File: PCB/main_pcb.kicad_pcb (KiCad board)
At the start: 2 copper layers, 116.9 x 116.9 mm, 37 parts, among them P1 SEN, P2 SRV, P3 PWR, P4 LED, P5 M1, P6 M2, Q1 5LN01SP, U1 Teensy_3.1, U2 RFM69_Breakout, U3 MCP6004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

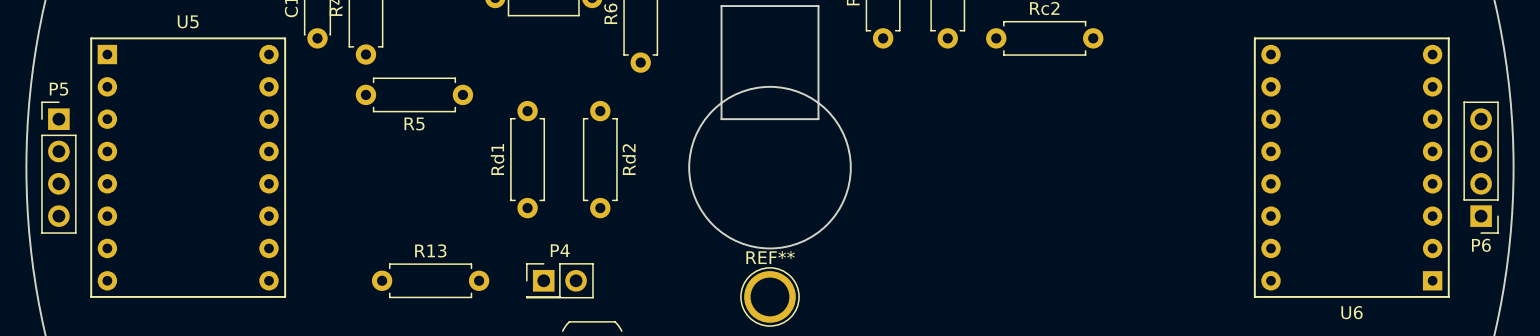
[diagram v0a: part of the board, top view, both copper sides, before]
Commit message: Added supporting PCB layouts
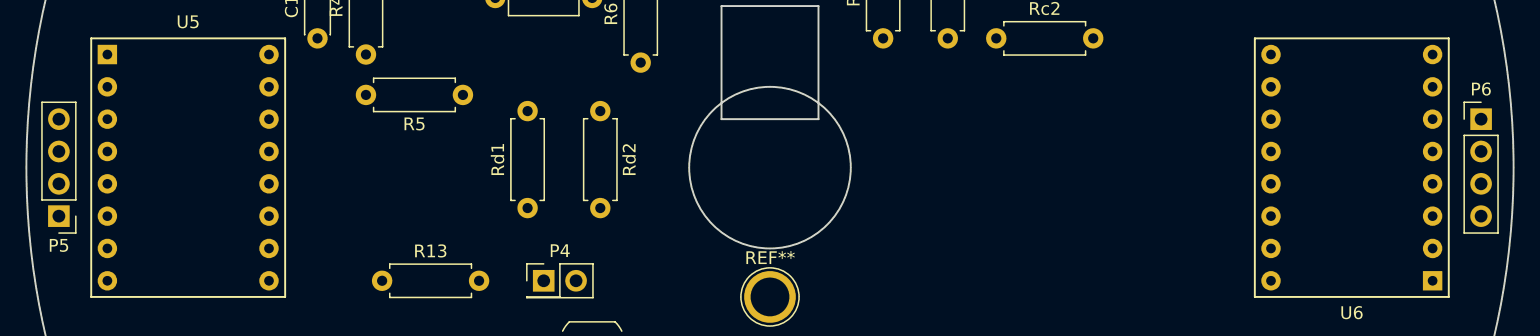
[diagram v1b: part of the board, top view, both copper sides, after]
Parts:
- moved P5 7.62 mm to (82.5, 99.1), turned to 180 degrees
- moved P6 7.62 mm to (194.3, 91.4), turned to 0 degrees
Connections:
- U5 pad 10: GND -> Net-(U5-Pad10)
- U5 pad 11: Net-(P5-Pad1) -> Net-(P5-Pad4)
- U5 pad 12: Net-(P5-Pad2) -> Net-(P5-Pad3)
- U5 pad 13: Net-(P5-Pad3) -> Net-(P5-Pad2)
- U5 pad 14: Net-(P5-Pad4) -> Net-(P5-Pad1)
- U5 pad 15: Net-(U5-Pad15) -> GND
- U5 pad 16: GND -> VDD
- U5 pad 9: VDD -> GND
- U6 pad 10: GND -> Net-(U6-Pad10)
- U6 pad 11: Net-(P6-Pad1) -> Net-(P6-Pad4)
- U6 pad 12: Net-(P6-Pad2) -> Net-(P6-Pad3)
- U6 pad 13: Net-(P6-Pad3) -> Net-(P6-Pad2)
- U6 pad 14: Net-(P6-Pad4) -> Net-(P6-Pad1)
- U6 pad 15: Net-(U6-Pad15) -> GND
- U6 pad 16: GND -> VDD
- U6 pad 9: VDD -> GND

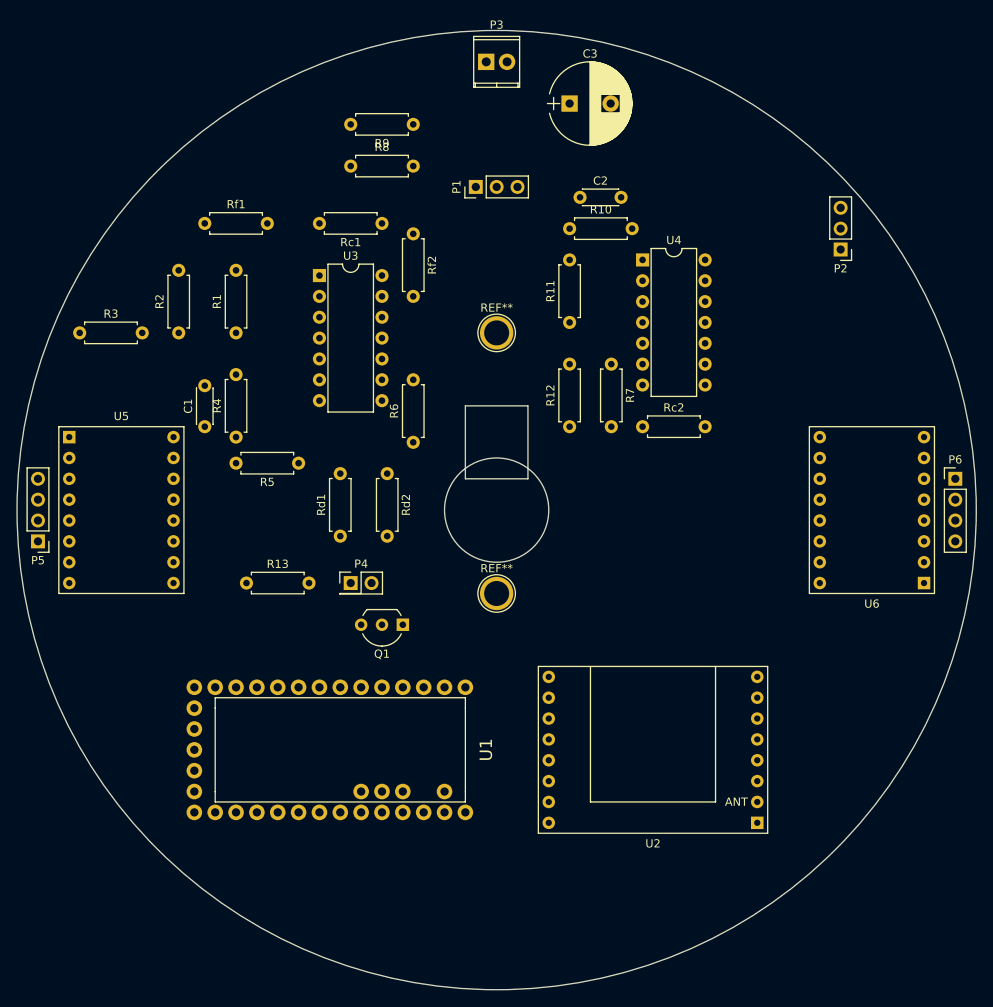
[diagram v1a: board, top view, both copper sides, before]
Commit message: Improved simulation, did most of the pcb trace layout
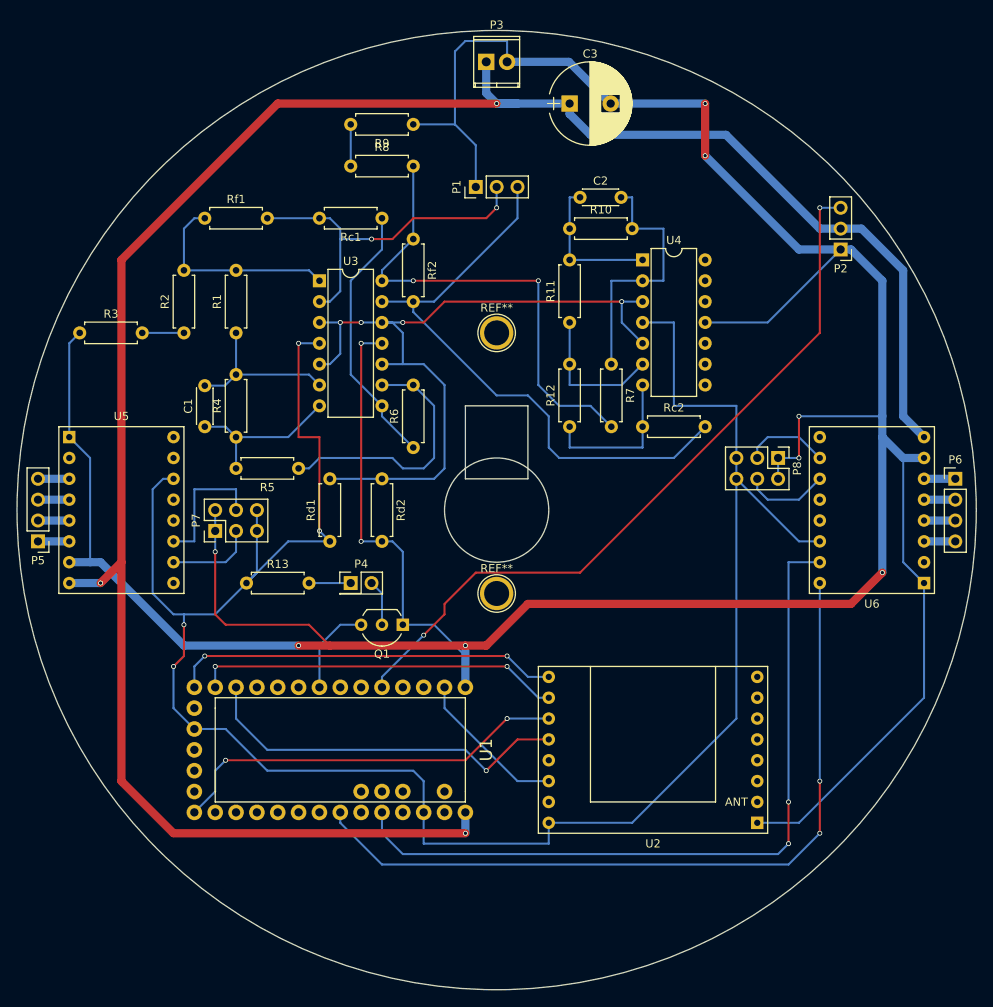
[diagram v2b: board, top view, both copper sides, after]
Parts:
- added P7: CONN_02X03, Pin_Headers:Pin_Header_Straight_2x03_Pitch2.54mm, F.Cu at (104.1, 97.8)
- added P8: CONN_02X03, Pin_Headers:Pin_Header_Straight_2x03_Pitch2.54mm, F.Cu at (172.7, 88.9)
- moved Rd1 1.42 mm to (118.1, 99.1)
- moved Rd2 0.90 mm to (124.5, 91.4)
- moved R2 0.64 mm to (100.3, 73.7)
- moved R5 0.64 mm to (114.3, 90.2)
- moved Rc1 0.64 mm to (124.5, 59.7)
- moved Rf1 0.64 mm to (102.9, 59.7)
- moved U3 0.64 mm to (116.8, 67.3)
- moved Rf2 0.63 mm to (128.3, 62.2)
- moved R6 0.63 mm to (128.3, 87.6)
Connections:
- U1 pad 31: Net-(U1-Pad31) -> +3V3
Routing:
- net GND: track 0.00 -> 455.6 mm, vias 0 -> 10
- net VDD: track 0.00 -> 259.8 mm, vias 0 -> 3
- net +3V3: track 0.00 -> 253.9 mm, vias 0 -> 4
- net /DIR2: track 0.00 -> 93.9 mm, vias 0 -> 2
- net /AnalogFilter1/Vref: track 0.00 -> 93.6 mm, vias 0 -> 4
- net /STEP2: track 0.00 -> 91.7 mm, vias 0 -> 2
- net /SRV: track 0.00 -> 90.5 mm, vias 0 -> 2
- net /AnalogFilter2/Sen: track 0.00 -> 72.5 mm
- net Net-(R7-Pad2): track 0.00 -> 58.3 mm, vias 0 -> 2
- net /SCK: track 0.00 -> 49.4 mm, vias 0 -> 2
- net /MISO: track 0.00 -> 47.3 mm, vias 0 -> 2
- net /RadCS: track 0.00 -> 46.1 mm, vias 0 -> 1
- net /MOSI: track 0.00 -> 44.8 mm, vias 0 -> 2
- net /AnalogFilter1/Sen: track 0.00 -> 43.3 mm, vias 0 -> 2
- net Net-(R6-Pad1): track 0.00 -> 32.7 mm
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
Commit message: Pulled in RFM69 library, modified to support teensy
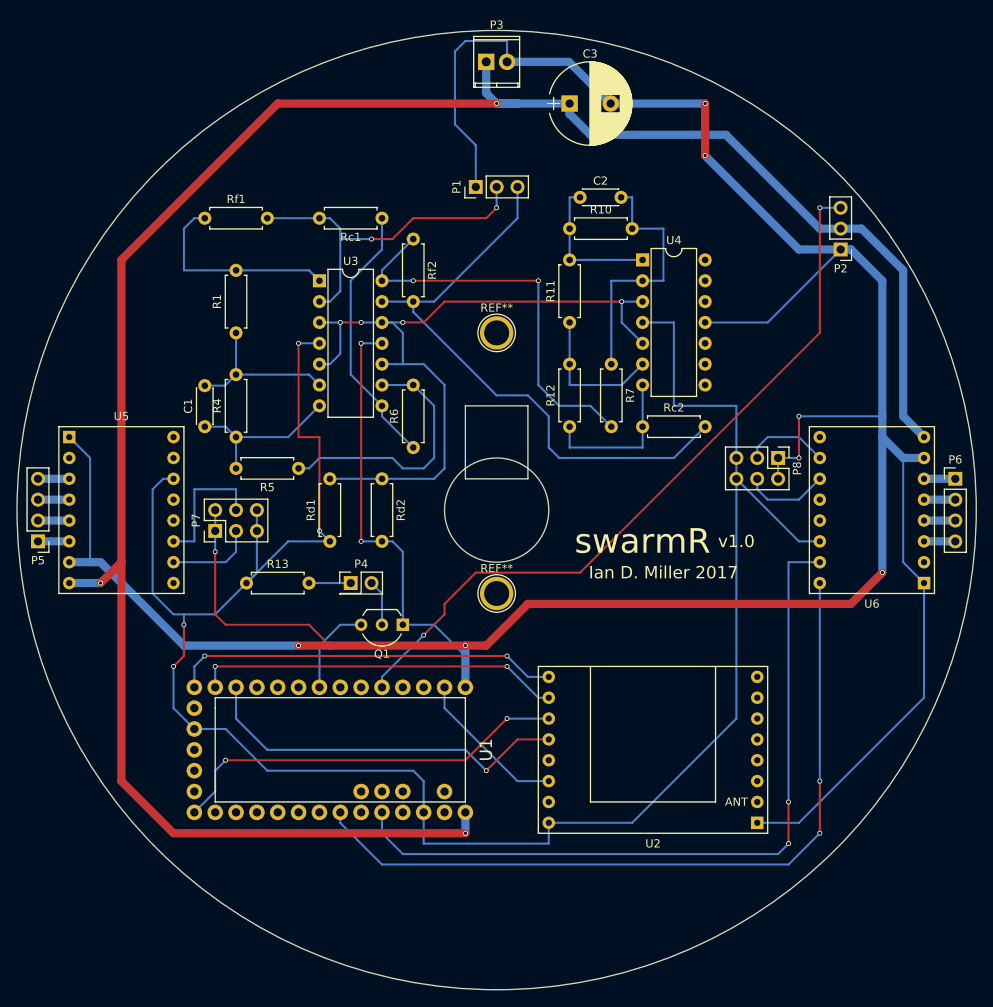
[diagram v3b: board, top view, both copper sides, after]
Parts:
- removed R2, R8: 4.3k, Resistors_ThroughHole:R_Axial_DIN0207_L6.3mm_D2.5mm_P7.62mm_Horizontal
- removed R3, R9: 3k, Resistors_ThroughHole:R_Axial_DIN0207_L6.3mm_D2.5mm_P7.62mm_Horizontal
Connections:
- R1 pad 2: Net-(R1-Pad2) -> /AnalogFilter1/Out
- R7 pad 2: Net-(R7-Pad2) -> /AnalogFilter2/Out
- Rf1 pad 1: Net-(R1-Pad2) -> /AnalogFilter1/Out
- Rf2 pad 1: Net-(R7-Pad2) -> /AnalogFilter2/Out
- U3 pad 1: Net-(R1-Pad2) -> /AnalogFilter1/Out
- U3 pad 14: Net-(R7-Pad2) -> /AnalogFilter2/Out
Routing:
- net Net-(R7-Pad2): track 58.3 -> 0.00 mm, vias 2 -> 0
- net /AnalogFilter2/Out: track 5.08 -> 49.4 mm, vias 0 -> 2
- net Net-(R1-Pad2): track 25.2 -> 0.00 mm
- net /AnalogFilter1/Out: track 5.08 -> 25.2 mm
- net GND: track 455.6 -> 437.3 mm
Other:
- board text added: "Ian D. Miller 2017"
- board text added: "swarmR"
- board text added: "v1.0"
